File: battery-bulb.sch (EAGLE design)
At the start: 12 parts, among them J1 USB-MICROB, U1 MCP73831, U2 RT9013-XXXB

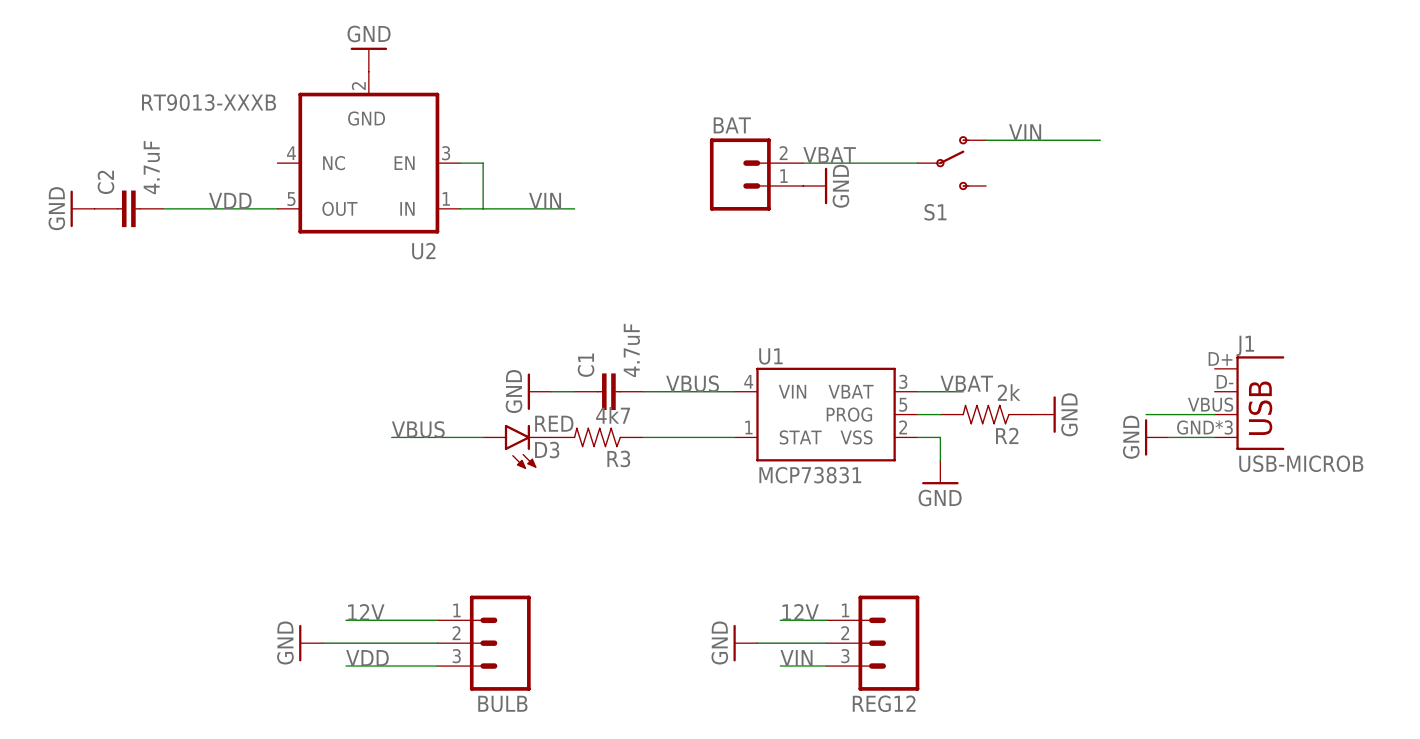
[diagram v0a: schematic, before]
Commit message: board revision 2
extend the board with direct connection to the bulb's logic board
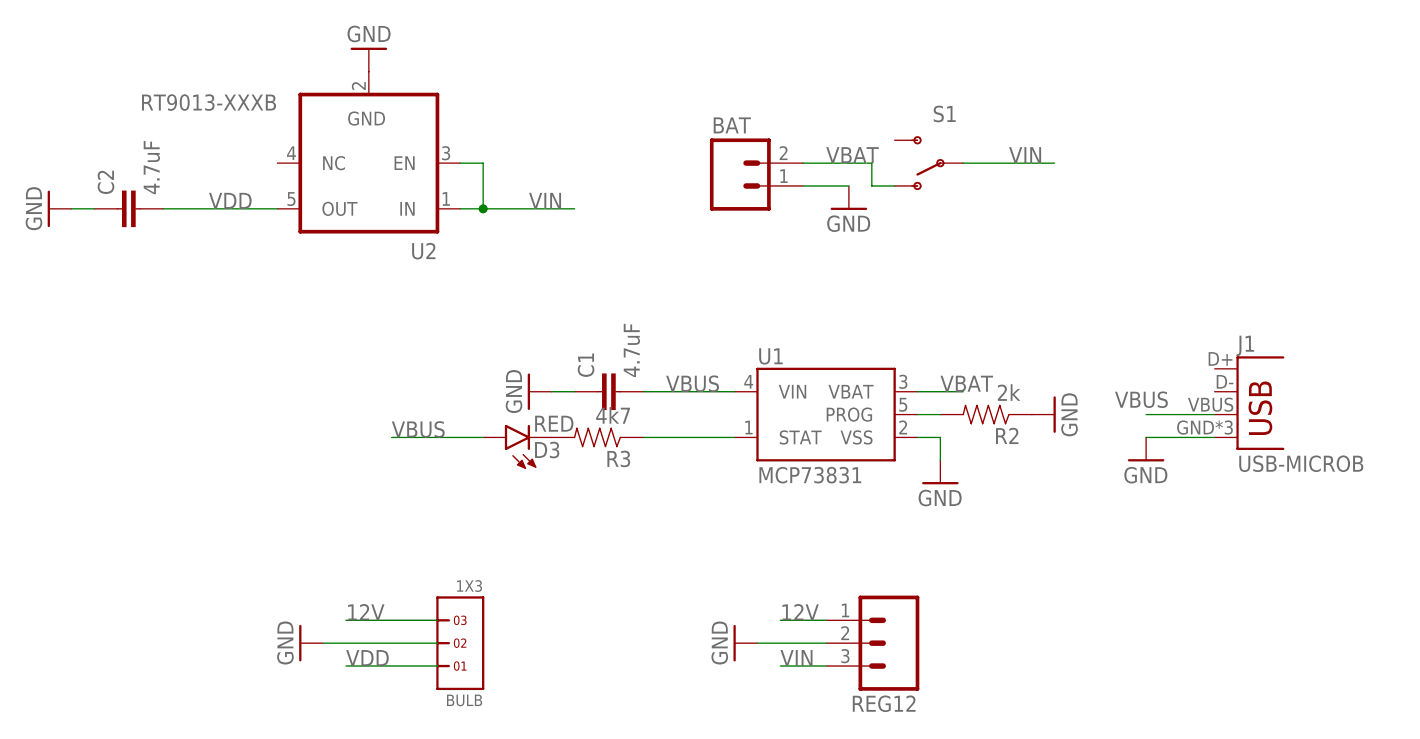
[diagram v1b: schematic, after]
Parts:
- BULB: value (none) -> 1X3; device SparkFun-Connectors:M03LOCK -> headers(2mm):1X3
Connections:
- net 12V: now also BULB.3; no longer BULB.1
- net VBAT: now also S1.O; no longer S1.P
- net VDD: now also BULB.1, C2.2; no longer BULB.3
- net VIN: now also S1.P; no longer S1.O
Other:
- moved on the sheet: S1
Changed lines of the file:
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@@
 <part name="REG12" library="SparkFun-Connectors" deviceset="M03" device="LOCK"/>
 <part name="GND1" library="SparkFun-Aesthetics" deviceset="GND" device=""/>
-<part name="BULB" library="SparkFun-Connectors" deviceset="M03" device="LOCK"/>
 <part name="GND2" library="SparkFun-Aesthetics" deviceset="GND" device=""/>
+<part name="BULB" library="headers(2mm)" deviceset="1X3" device=""/>
 </parts>
 <sheets>
@@
 </plain>
 <instances>
-<instance part="GND4" gate="1" x="55.88" y="111.76" rot="R90"/>
+<instance part="GND4" gate="1" x="58.42" y="109.22"/>
 <instance part="BAT" gate="G$1" x="45.72" y="111.76"/>
-<instance part="S1" gate="1" x="68.58" y="114.3"/>
+<instance part="S1" gate="1" x="68.58" y="114.3" rot="R180"/>
 <instance part="U1" gate="G$1" x="55.88" y="86.36"/>
 <instance part="J1" gate="G$1" x="101.6" y="83.82"/>
-<instance part="GND6" gate="1" x="91.44" y="83.82" rot="R270"/>
+<instance part="GND6" gate="1" x="91.44" y="81.28"/>
 <instance part="C1" gate="G$1" x="33.02" y="88.9" rot="R90"/>
 <instance part="GND7" gate="1" x="22.86" y="88.9" smashed="yes" rot="R270">
@@
 </instance>
 <instance part="C2" gate="G$1" x="-20.32" y="109.22" rot="R90"/>
-<instance part="GND8" gate="1" x="-27.94" y="109.22" rot="R270"/>
+<instance part="GND8" gate="1" x="-30.48" y="109.22" rot="R270"/>
 <instance part="R2" gate="G$1" x="73.66" y="86.36" rot="R180"/>
 <instance part="GND9" gate="1" x="81.28" y="86.36" rot="R90"/>
@@
 <instance part="REG12" gate="J$1" x="63.5" y="60.96" rot="R180"/>
 <instance part="GND1" gate="1" x="45.72" y="60.96" rot="R270"/>
-<instance part="BULB" gate="J$1" x="20.32" y="60.96" rot="R180"/>
 <instance part="GND2" gate="1" x="-2.54" y="60.96" rot="R270"/>
+<instance part="BULB" gate="G$1" x="15.24" y="60.96" rot="R180"/>
 </instances>
 <busses>
@@
 <net name="VDD" class="0">
 <segment>
-<pinref part="U2" gate="G$1" pin="OUT"/>
-<wire x1="-5.08" y1="109.22" x2="-17.78" y2="109.22" width="0.1524" layer="91"/>
-<label x="-12.7" y="109.22" size="1.778" layer="95"/>
+<wire x1="12.7" y1="58.42" x2="2.54" y2="58.42" width="0.1524" layer="91"/>
+<label x="2.54" y="58.42" size="1.778" layer="95"/>
+<pinref part="BULB" gate="G$1" pin="1"/>
 </segment>
 <segment>
-<pinref part="BULB" gate="J$1" pin="3"/>
-<wire x1="12.7" y1="58.42" x2="2.54" y2="58.42" width="0.1524" layer="91"/>
-<label x="2.54" y="58.42" size="1.778" layer="95"/>
+<pinref part="C2" gate="G$1" pin="2"/>
+<pinref part="U2" gate="G$1" pin="OUT"/>
+<wire x1="-17.78" y1="109.22" x2="-5.08" y2="109.22" width="0.1524" layer="91"/>
+<label x="-12.7" y="109.22" size="1.778" layer="95"/>
 </segment>
 </net>
@@
 <pinref part="GND6" gate="1" pin="GND"/>
 <pinref part="J1" gate="G$1" pin="GND"/>
-<wire x1="93.98" y1="83.82" x2="99.06" y2="83.82" width="0.1524" layer="91"/>
+<wire x1="91.44" y1="83.82" x2="99.06" y2="83.82" width="0.1524" layer="91"/>
 </segment>
 <segment>
@@
 <pinref part="BAT" gate="G$1" pin="1"/>
 <pinref part="GND4" gate="1" pin="GND"/>
+<wire x1="58.42" y1="111.76" x2="53.34" y2="111.76" width="0.1524" layer="91"/>
 </segment>
 <segment>
 <pinref part="GND8" gate="1" pin="GND"/>
 <pinref part="C2" gate="G$1" pin="1"/>
+<wire x1="-27.94" y1="109.22" x2="-25.4" y2="109.22" width="0.1524" layer="91"/>
 </segment>
 <segment>
@@
 <segment>
 <pinref part="GND2" gate="1" pin="GND"/>
-<pinref part="BULB" gate="J$1" pin="2"/>
 <wire x1="0" y1="60.96" x2="12.7" y2="60.96" width="0.1524" layer="91"/>
+<pinref part="BULB" gate="G$1" pin="2"/>
 </segment>
 </net>
@@
 <wire x1="15.24" y1="114.3" x2="17.78" y2="114.3" width="0.1524" layer="91"/>
 <wire x1="17.78" y1="114.3" x2="17.78" y2="109.22" width="0.1524" layer="91"/>
-</segment>
-<segment>
-<pinref part="S1" gate="1" pin="O"/>
-<wire x1="73.66" y1="116.84" x2="86.36" y2="116.84" width="0.1524" layer="91"/>
-<label x="76.2" y="116.84" size="1.778" layer="95"/>
+<junction x="17.78" y="109.22"/>
 </segment>
 <segment>
@@
 <label x="50.8" y="58.42" size="1.778" layer="95"/>
 </segment>
+<segment>
+<pinref part="S1" gate="1" pin="P"/>
+<wire x1="71.12" y1="114.3" x2="81.28" y2="114.3" width="0.1524" layer="91"/>
+<label x="76.2" y="114.3" size="1.778" layer="95"/>
+</segment>
 </net>
 <net name="VBUS" class="0">
@@
 <pinref part="J1" gate="G$1" pin="VBUS"/>
 <wire x1="99.06" y1="86.36" x2="91.44" y2="86.36" width="0.1524" layer="91"/>
+<label x="93.98" y="88.9" size="1.778" layer="95" rot="R180"/>
 </segment>
 <segment>
@@
 <segment>
 <pinref part="BAT" gate="G$1" pin="2"/>
-<pinref part="S1" gate="1" pin="P"/>
-<wire x1="53.34" y1="114.3" x2="66.04" y2="114.3" width="0.1524" layer="91"/>
-<label x="53.34" y="114.3" size="1.778" layer="95"/>
+<wire x1="53.34" y1="114.3" x2="60.96" y2="114.3" width="0.1524" layer="91"/>
+<wire x1="60.96" y1="114.3" x2="60.96" y2="111.76" width="0.1524" layer="91"/>
+<pinref part="S1" gate="1" pin="O"/>
+<wire x1="60.96" y1="111.76" x2="63.5" y2="111.76" width="0.1524" layer="91"/>
+<label x="55.88" y="114.3" size="1.778" layer="95"/>
 </segment>
 </net>
@@
 <net name="12V" class="0">
 <segment>
-<pinref part="BULB" gate="J$1" pin="1"/>
 <wire x1="12.7" y1="63.5" x2="2.54" y2="63.5" width="0.1524" layer="91"/>
 <label x="2.54" y="63.5" size="1.778" layer="95"/>
+<pinref part="BULB" gate="G$1" pin="3"/>
 </segment>
 <segment>
